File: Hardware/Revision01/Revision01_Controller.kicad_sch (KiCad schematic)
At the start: 7 parts, among them U1 NUCLEO-L476RG

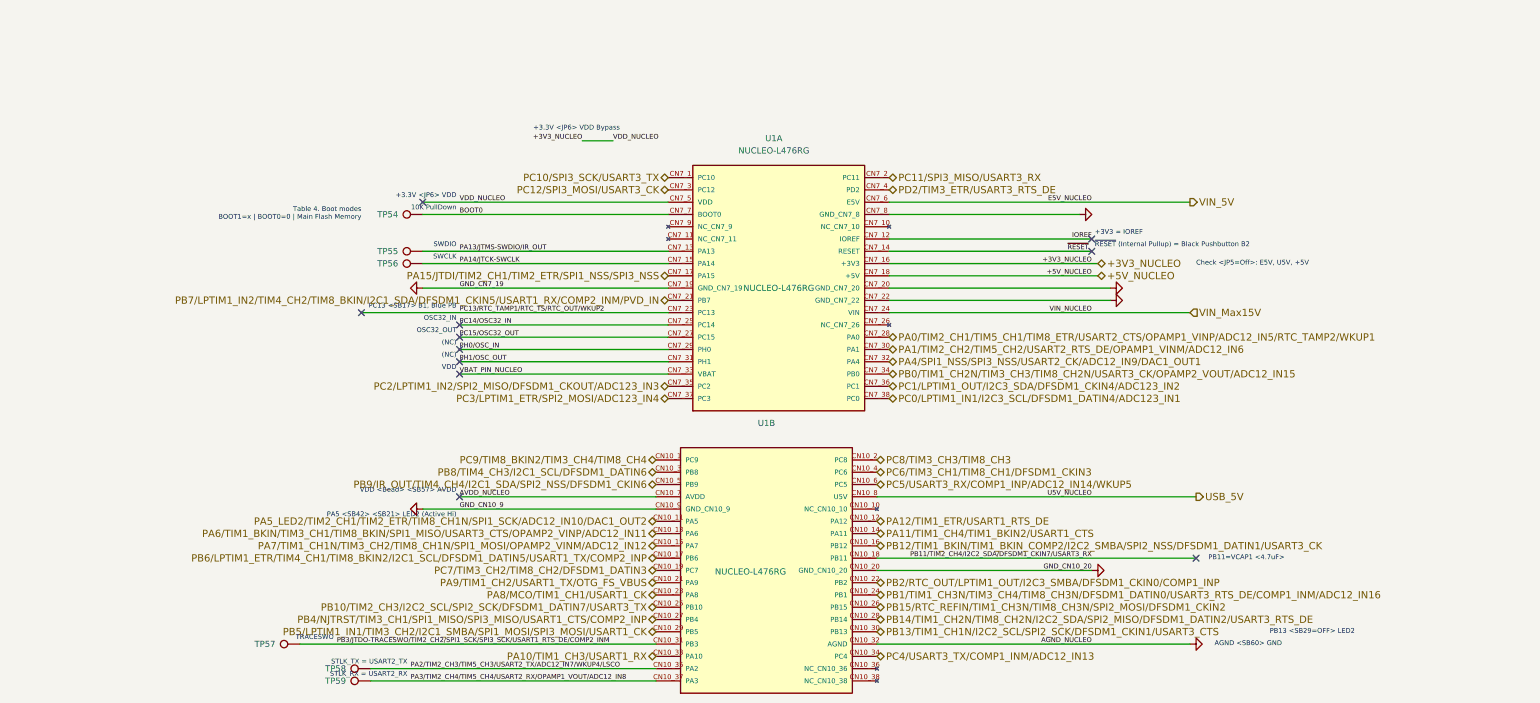
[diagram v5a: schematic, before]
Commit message: ADDED 25pF to STRAIN GAUGES to remove noise ADDED FOOTPRINTS TO COMPONENTS Changed PS back to external-highside switch as internal mosfet current rating is too low pull-up for PMOS strainV_enable added Reconfigured new Nucleo board STM32IDE file
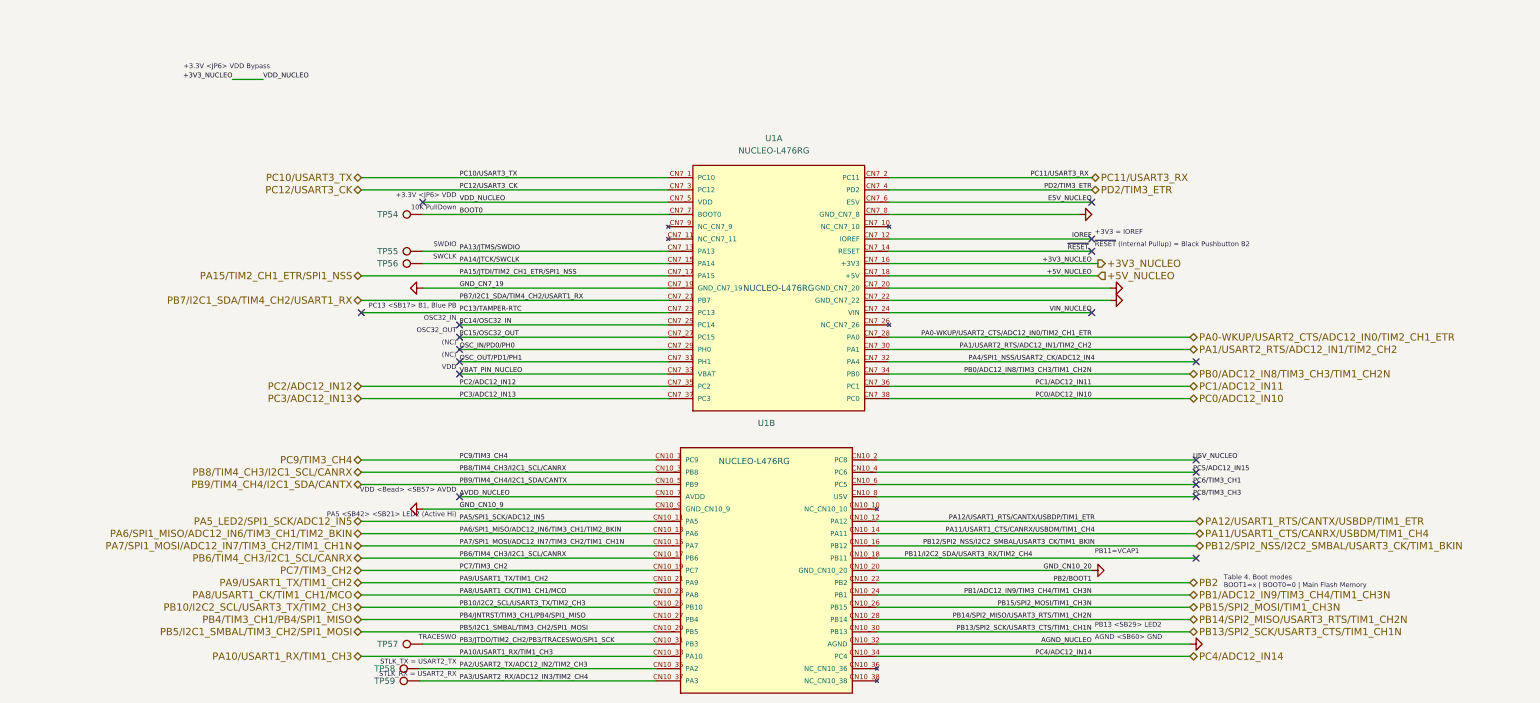
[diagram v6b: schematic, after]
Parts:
- TP54, TP55, TP56, TP57, TP58, TP59: footprint (none) -> TestPoint:TestPoint_Pad_2.0x2.0mm
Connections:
- net PA0/TIM2_CH1/TIM5_CH1/TIM8_ETR/USART2_CTS/OPAMP1_VINP/ADC12_IN5/RTC_TAMP2/WKUP1 renamed PA0-WKUP/USART2_CTS/ADC12_IN0/TIM2_CH1_ETR
- net PA1/TIM2_CH2/TIM5_CH2/USART2_RTS_DE/OPAMP1_VINM/ADC12_IN6 renamed PA1/USART2_RTS/ADC12_IN1/TIM2_CH2
- net PA10/TIM1_CH3/USART1_RX renamed PA10/USART1_RX/TIM1_CH3
- net PA11/TIM1_CH4/TIM1_BKIN2/USART1_CTS renamed PA11/USART1_CTS/CANRX/USBDM/TIM1_CH4
- net PA12/TIM1_ETR/USART1_RTS_DE renamed PA12/USART1_RTS/CANTX/USBDP/TIM1_ETR
- net PA13/JTMS-SWDIO/IR_OUT renamed PA13/JTMS/SWDIO
- net PA14/JTCK-SWCLK renamed PA14/JTCK/SWCLK
- net PA15/JTDI/TIM2_CH1/TIM2_ETR/SPI1_NSS/SPI3_NSS renamed PA15/TIM2_CH1_ETR/SPI1_NSS
- net PA2/TIM2_CH3/TIM5_CH3/USART2_TX/ADC12_IN7/WKUP4/LSCO renamed PA2/USART2_TX/ADC12_IN2/TIM2_CH3
- net PA3/TIM2_CH4/TIM5_CH4/USART2_RX/OPAMP1_VOUT/ADC12_IN8 renamed PA3/USART2_RX/ADC12_IN3/TIM2_CH4
- net PA4/SPI1_NSS/SPI3_NSS/USART2_CK/ADC12_IN9/DAC1_OUT1 renamed PA4/SPI1_NSS/USART2_CK/ADC12_IN4
- net PA5_LED2/TIM2_CH1/TIM2_ETR/TIM8_CH1N/SPI1_SCK/ADC12_IN10/DAC1_OUT2 renamed PA5_LED2/SPI1_SCK/ADC12_IN5
- net PA6/TIM1_BKIN/TIM3_CH1/TIM8_BKIN/SPI1_MISO/USART3_CTS/OPAMP2_VINP/ADC12_IN11 renamed PA6/SPI1_MISO/ADC12_IN6/TIM3_CH1/TIM2_BKIN
- net PA7/TIM1_CH1N/TIM3_CH2/TIM8_CH1N/SPI1_MOSI/OPAMP2_VINM/ADC12_IN12 renamed PA7/SPI1_MOSI/ADC12_IN7/TIM3_CH2/TIM1_CH1N
- net PA8/MCO/TIM1_CH1/USART1_CK renamed PA8/USART1_CK/TIM1_CH1/MCO
- net PA9/TIM1_CH2/USART1_TX/OTG_FS_VBUS renamed PA9/USART1_TX/TIM1_CH2
- net PB0/TIM1_CH2N/TIM3_CH3/TIM8_CH2N/USART3_CK/OPAMP2_VOUT/ADC12_IN15 renamed PB0/ADC12_IN8/TIM3_CH3/TIM1_CH2N
- net PB1/TIM1_CH3N/TIM3_CH4/TIM8_CH3N/DFSDM1_DATIN0/USART3_RTS_DE/COMP1_INM/ADC12_IN16 renamed PB1/ADC12_IN9/TIM3_CH4/TIM1_CH3N
- net PB10/TIM2_CH3/I2C2_SCL/SPI2_SCK/DFSDM1_DATIN7/USART3_TX renamed PB10/I2C2_SCL/USART3_TX/TIM2_CH3
- net PB11/TIM2_CH4/I2C2_SDA/DFSDM1_CKIN7/USART3_RX renamed PB11/I2C2_SDA/USART3_RX/TIM2_CH4
- net PB12/TIM1_BKIN/TIM1_BKIN_COMP2/I2C2_SMBA/SPI2_NSS/DFSDM1_DATIN1/USART3_CK renamed PB12/SPI2_NSS/I2C2_SMBAL/USART3_CK/TIM1_BKIN
- net PB13/TIM1_CH1N/I2C2_SCL/SPI2_SCK/DFSDM1_CKIN1/USART3_CTS renamed PB13/SPI2_SCK/USART3_CTS/TIM1_CH1N
- net PB14/TIM1_CH2N/TIM8_CH2N/I2C2_SDA/SPI2_MISO/DFSDM1_DATIN2/USART3_RTS_DE renamed PB14/SPI2_MISO/USART3_RTS/TIM1_CH2N
- net PB15/RTC_REFIN/TIM1_CH3N/TIM8_CH3N/SPI2_MOSI/DFSDM1_CKIN2 renamed PB15/SPI2_MOSI/TIM1_CH3N
- net PB2/RTC_OUT/LPTIM1_OUT/I2C3_SMBA/DFSDM1_CKIN0/COMP1_INP renamed PB2
- net PB3/JTDO-TRACESWO/TIM2_CH2/SPI1_SCK/SPI3_SCK/USART1_RTS_DE/COMP2_INM renamed PB3/JTDO/TIM2_CH2/PB3/TRACESWO/SPI1_SCK
- net PB4/NJTRST/TIM3_CH1/SPI1_MISO/SPI3_MISO/USART1_CTS/COMP2_INP renamed PB4/TIM3_CH1/PB4/SPI1_MISO
- net PB5/LPTIM1_IN1/TIM3_CH2/I2C1_SMBA/SPI1_MOSI/SPI3_MOSI/USART1_CK renamed PB5/I2C1_SMBAL/TIM3_CH2/SPI1_MOSI
- net PB6/LPTIM1_ETR/TIM4_CH1/TIM8_BKIN2/I2C1_SCL/DFSDM1_DATIN5/USART1_TX/COMP2_INP renamed PB6/TIM4_CH3/I2C1_SCL/CANRX
- net PB7/LPTIM1_IN2/TIM4_CH2/TIM8_BKIN/I2C1_SDA/DFSDM1_CKIN5/USART1_RX/COMP2_INM/PVD_IN renamed PB7/I2C1_SDA/TIM4_CH2/USART1_RX
- net PB8/TIM4_CH3/I2C1_SCL/DFSDM1_DATIN6 renamed PB8/TIM4_CH3/I2C1_SCL/CANRX
- net PB9/IR_OUT/TIM4_CH4/I2C1_SDA/SPI2_NSS/DFSDM1_CKIN6 renamed PB9/TIM4_CH4/I2C1_SDA/CANTX
- net PC0/LPTIM1_IN1/I2C3_SCL/DFSDM1_DATIN4/ADC123_IN1 renamed PC0/ADC12_IN10
- net PC1/LPTIM1_OUT/I2C3_SDA/DFSDM1_CKIN4/ADC123_IN2 renamed PC1/ADC12_IN11
- net PC10/SPI3_SCK/USART3_TX renamed PC10/USART3_TX
- net PC11/SPI3_MISO/USART3_RX renamed PC11/USART3_RX
- net PC12/SPI3_MOSI/USART3_CK renamed PC12/USART3_CK
- net PC13/RTC_TAMP1/RTC_TS/RTC_OUT/WKUP2 renamed PC13/TAMPER-RTC
- net PC2/LPTIM1_IN2/SPI2_MISO/DFSDM1_CKOUT/ADC123_IN3 renamed PC2/ADC12_IN12
- net PC3/LPTIM1_ETR/SPI2_MOSI/ADC123_IN4 renamed PC3/ADC12_IN13
- net PC4/USART3_TX/COMP1_INM/ADC12_IN13 renamed PC4/ADC12_IN14
- net PC5/USART3_RX/COMP1_INP/ADC12_IN14/WKUP5 renamed PC6/TIM3_CH1
- net PC6/TIM3_CH1/TIM8_CH1/DFSDM1_CKIN3 renamed PC5/ADC12_IN15
- net PC7/TIM3_CH2/TIM8_CH2/DFSDM1_DATIN3 renamed PC7/TIM3_CH2
- net PC8/TIM3_CH3/TIM8_CH3 renamed U5V_NUCLEO
- net PC9/TIM8_BKIN2/TIM3_CH4/TIM8_CH4 renamed PC9/TIM3_CH4
- net PD2/TIM3_ETR/USART3_RTS_DE renamed PD2/TIM3_ETR
- net PH0/OSC_IN renamed OSC_IN/PD0/PH0
- net PH1/OSC_OUT renamed OSC_OUT/PD1/PH1
- net USB_5V renamed PC8/TIM3_CH3
- net VIN_5V renamed E5V_NUCLEO
- net VIN_Max15V renamed VIN_NUCLEO
- no-connect marks 11 -> 18
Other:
- note added: "PB11=VCAP1"
- note added: "PB13 <SB29> LED2"
- note removed: "Check <JP5=Off>: E5V, U5V, +5V"
- note removed: "PB11=VCAP1 <4.7uF>"
- note removed: "PB13 <SB29=OFF> LED2"
- moved on the sheet: TP57, TP58, TP59

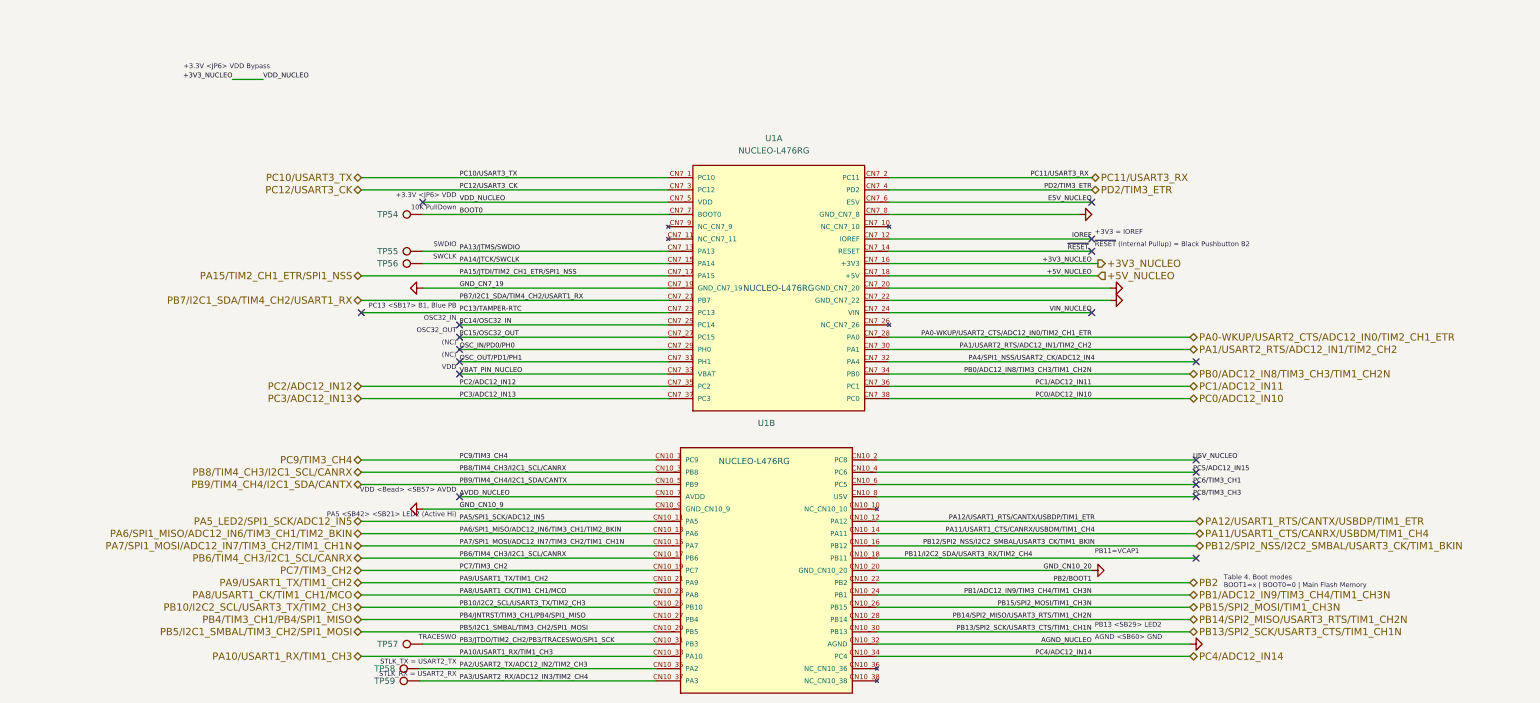
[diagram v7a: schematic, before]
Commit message: INTEGRATED MCU_SHEET INTO MAIN SHEET
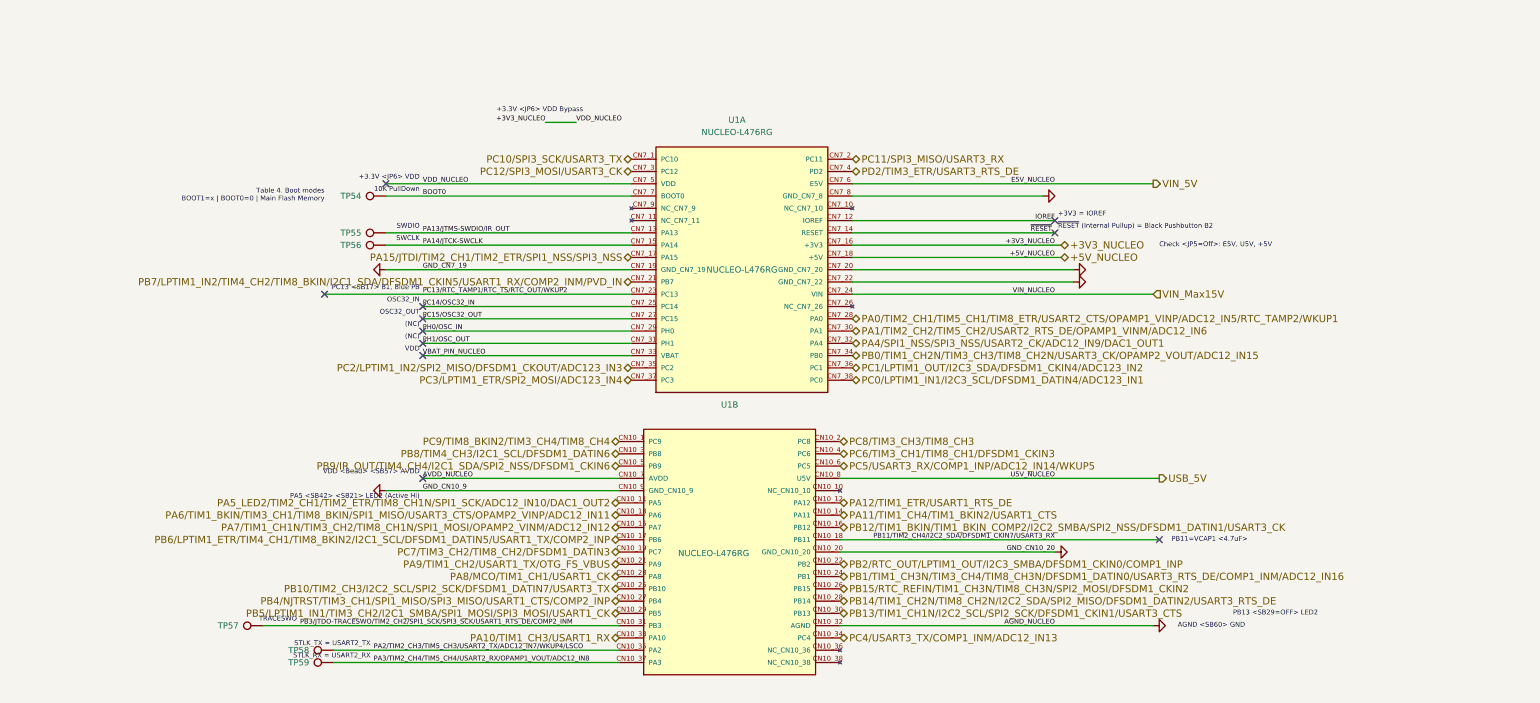
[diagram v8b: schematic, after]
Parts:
- TP54, TP55, TP56, TP57, TP58, TP59: footprint TestPoint:TestPoint_Pad_2.0x2.0mm -> (none)
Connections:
- net E5V_NUCLEO renamed VIN_5V
- net OSC_IN/PD0/PH0 renamed PH0/OSC_IN
- net OSC_OUT/PD1/PH1 renamed PH1/OSC_OUT
- net PA0-WKUP/USART2_CTS/ADC12_IN0/TIM2_CH1_ETR renamed PA0/TIM2_CH1/TIM5_CH1/TIM8_ETR/USART2_CTS/OPAMP1_VINP/ADC12_IN5/RTC_TAMP2/WKUP1
- net PA10/USART1_RX/TIM1_CH3 renamed PA10/TIM1_CH3/USART1_RX
- net PA11/USART1_CTS/CANRX/USBDM/TIM1_CH4 renamed PA11/TIM1_CH4/TIM1_BKIN2/USART1_CTS
- net PA12/USART1_RTS/CANTX/USBDP/TIM1_ETR renamed PA12/TIM1_ETR/USART1_RTS_DE
- net PA13/JTMS/SWDIO renamed PA13/JTMS-SWDIO/IR_OUT
- net PA14/JTCK/SWCLK renamed PA14/JTCK-SWCLK
- net PA15/TIM2_CH1_ETR/SPI1_NSS renamed PA15/JTDI/TIM2_CH1/TIM2_ETR/SPI1_NSS/SPI3_NSS
- net PA1/USART2_RTS/ADC12_IN1/TIM2_CH2 renamed PA1/TIM2_CH2/TIM5_CH2/USART2_RTS_DE/OPAMP1_VINM/ADC12_IN6
- net PA2/USART2_TX/ADC12_IN2/TIM2_CH3 renamed PA2/TIM2_CH3/TIM5_CH3/USART2_TX/ADC12_IN7/WKUP4/LSCO
- net PA3/USART2_RX/ADC12_IN3/TIM2_CH4 renamed PA3/TIM2_CH4/TIM5_CH4/USART2_RX/OPAMP1_VOUT/ADC12_IN8
- net PA4/SPI1_NSS/USART2_CK/ADC12_IN4 renamed PA4/SPI1_NSS/SPI3_NSS/USART2_CK/ADC12_IN9/DAC1_OUT1
- net PA5_LED2/SPI1_SCK/ADC12_IN5 renamed PA5_LED2/TIM2_CH1/TIM2_ETR/TIM8_CH1N/SPI1_SCK/ADC12_IN10/DAC1_OUT2
- net PA6/SPI1_MISO/ADC12_IN6/TIM3_CH1/TIM2_BKIN renamed PA6/TIM1_BKIN/TIM3_CH1/TIM8_BKIN/SPI1_MISO/USART3_CTS/OPAMP2_VINP/ADC12_IN11
- net PA7/SPI1_MOSI/ADC12_IN7/TIM3_CH2/TIM1_CH1N renamed PA7/TIM1_CH1N/TIM3_CH2/TIM8_CH1N/SPI1_MOSI/OPAMP2_VINM/ADC12_IN12
- net PA8/USART1_CK/TIM1_CH1/MCO renamed PA8/MCO/TIM1_CH1/USART1_CK
- net PA9/USART1_TX/TIM1_CH2 renamed PA9/TIM1_CH2/USART1_TX/OTG_FS_VBUS
- net PB0/ADC12_IN8/TIM3_CH3/TIM1_CH2N renamed PB0/TIM1_CH2N/TIM3_CH3/TIM8_CH2N/USART3_CK/OPAMP2_VOUT/ADC12_IN15
- net PB10/I2C2_SCL/USART3_TX/TIM2_CH3 renamed PB10/TIM2_CH3/I2C2_SCL/SPI2_SCK/DFSDM1_DATIN7/USART3_TX
- net PB11/I2C2_SDA/USART3_RX/TIM2_CH4 renamed PB11/TIM2_CH4/I2C2_SDA/DFSDM1_CKIN7/USART3_RX
- net PB12/SPI2_NSS/I2C2_SMBAL/USART3_CK/TIM1_BKIN renamed PB12/TIM1_BKIN/TIM1_BKIN_COMP2/I2C2_SMBA/SPI2_NSS/DFSDM1_DATIN1/USART3_CK
- net PB13/SPI2_SCK/USART3_CTS/TIM1_CH1N renamed PB13/TIM1_CH1N/I2C2_SCL/SPI2_SCK/DFSDM1_CKIN1/USART3_CTS
- net PB14/SPI2_MISO/USART3_RTS/TIM1_CH2N renamed PB14/TIM1_CH2N/TIM8_CH2N/I2C2_SDA/SPI2_MISO/DFSDM1_DATIN2/USART3_RTS_DE
- net PB15/SPI2_MOSI/TIM1_CH3N renamed PB15/RTC_REFIN/TIM1_CH3N/TIM8_CH3N/SPI2_MOSI/DFSDM1_CKIN2
- net PB1/ADC12_IN9/TIM3_CH4/TIM1_CH3N renamed PB1/TIM1_CH3N/TIM3_CH4/TIM8_CH3N/DFSDM1_DATIN0/USART3_RTS_DE/COMP1_INM/ADC12_IN16
- net PB2 renamed PB2/RTC_OUT/LPTIM1_OUT/I2C3_SMBA/DFSDM1_CKIN0/COMP1_INP
- net PB3/JTDO/TIM2_CH2/PB3/TRACESWO/SPI1_SCK renamed PB3/JTDO-TRACESWO/TIM2_CH2/SPI1_SCK/SPI3_SCK/USART1_RTS_DE/COMP2_INM
- net PB4/TIM3_CH1/PB4/SPI1_MISO renamed PB4/NJTRST/TIM3_CH1/SPI1_MISO/SPI3_MISO/USART1_CTS/COMP2_INP
- net PB5/I2C1_SMBAL/TIM3_CH2/SPI1_MOSI renamed PB5/LPTIM1_IN1/TIM3_CH2/I2C1_SMBA/SPI1_MOSI/SPI3_MOSI/USART1_CK
- net PB6/TIM4_CH3/I2C1_SCL/CANRX renamed PB6/LPTIM1_ETR/TIM4_CH1/TIM8_BKIN2/I2C1_SCL/DFSDM1_DATIN5/USART1_TX/COMP2_INP
- net PB7/I2C1_SDA/TIM4_CH2/USART1_RX renamed PB7/LPTIM1_IN2/TIM4_CH2/TIM8_BKIN/I2C1_SDA/DFSDM1_CKIN5/USART1_RX/COMP2_INM/PVD_IN
- net PB8/TIM4_CH3/I2C1_SCL/CANRX renamed PB8/TIM4_CH3/I2C1_SCL/DFSDM1_DATIN6
- net PB9/TIM4_CH4/I2C1_SDA/CANTX renamed PB9/IR_OUT/TIM4_CH4/I2C1_SDA/SPI2_NSS/DFSDM1_CKIN6
- net PC0/ADC12_IN10 renamed PC0/LPTIM1_IN1/I2C3_SCL/DFSDM1_DATIN4/ADC123_IN1
- net PC10/USART3_TX renamed PC10/SPI3_SCK/USART3_TX
- net PC11/USART3_RX renamed PC11/SPI3_MISO/USART3_RX
- net PC12/USART3_CK renamed PC12/SPI3_MOSI/USART3_CK
- net PC13/TAMPER-RTC renamed PC13/RTC_TAMP1/RTC_TS/RTC_OUT/WKUP2
- net PC1/ADC12_IN11 renamed PC1/LPTIM1_OUT/I2C3_SDA/DFSDM1_CKIN4/ADC123_IN2
- net PC2/ADC12_IN12 renamed PC2/LPTIM1_IN2/SPI2_MISO/DFSDM1_CKOUT/ADC123_IN3
- net PC3/ADC12_IN13 renamed PC3/LPTIM1_ETR/SPI2_MOSI/ADC123_IN4
- net PC4/ADC12_IN14 renamed PC4/USART3_TX/COMP1_INM/ADC12_IN13
- net PC5/ADC12_IN15 renamed PC6/TIM3_CH1/TIM8_CH1/DFSDM1_CKIN3
- net PC6/TIM3_CH1 renamed PC5/USART3_RX/COMP1_INP/ADC12_IN14/WKUP5
- net PC7/TIM3_CH2 renamed PC7/TIM3_CH2/TIM8_CH2/DFSDM1_DATIN3
- net PC8/TIM3_CH3 renamed USB_5V
- net PC9/TIM3_CH4 renamed PC9/TIM8_BKIN2/TIM3_CH4/TIM8_CH4
- net PD2/TIM3_ETR renamed PD2/TIM3_ETR/USART3_RTS_DE
- net U5V_NUCLEO renamed PC8/TIM3_CH3/TIM8_CH3
- net VIN_NUCLEO renamed VIN_Max15V
- no-connect marks 18 -> 11
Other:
- note added: "Check <JP5=Off>: E5V, U5V, +5V"
- note added: "PB11=VCAP1 <4.7uF>"
- note added: "PB13 <SB29=OFF> LED2"
- note removed: "PB11=VCAP1"
- note removed: "PB13 <SB29> LED2"
- moved on the sheet: TP54, TP55, TP56, TP57, TP58, TP59, U1A, U1B
